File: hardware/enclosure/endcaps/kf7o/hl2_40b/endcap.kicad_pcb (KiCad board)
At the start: 2 copper layers, 106 x 40 mm, 14 parts, among them Q1 DTC144E, Q2 IRLML6402

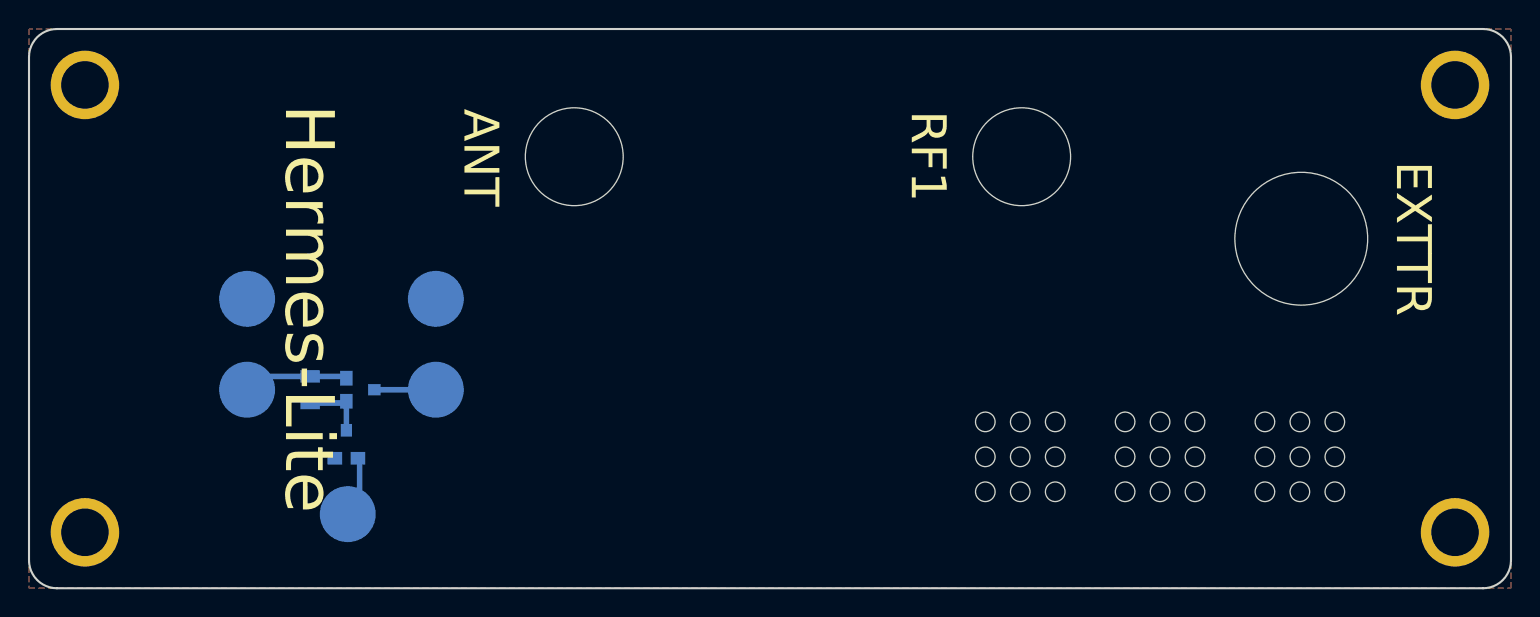
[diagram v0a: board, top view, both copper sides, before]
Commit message: Rev 2 of rear end plate
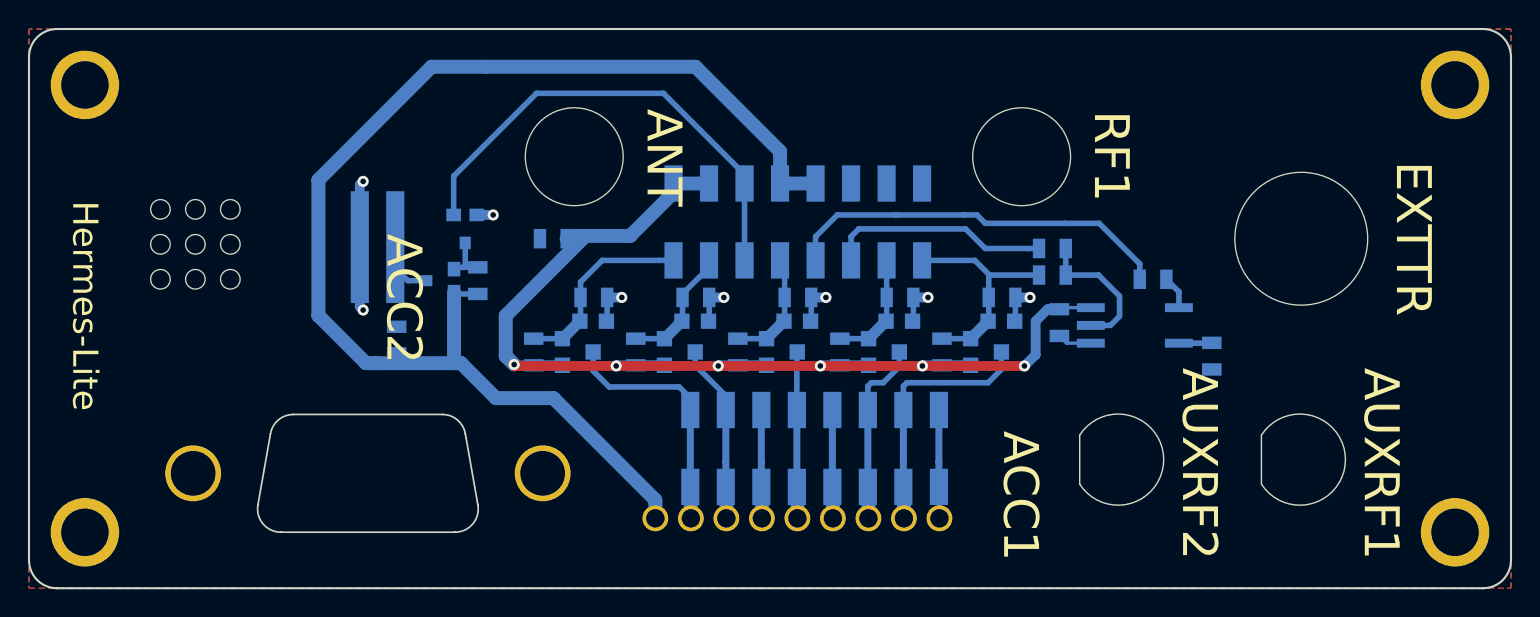
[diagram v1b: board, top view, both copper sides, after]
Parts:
- removed the REF** at (118.4, 83.1)
- removed TP1: Power, TestPoint:TestPoint_Pad_D4.0mm
- removed TP2: Fan Control, TestPoint:TestPoint_Pad_D4.0mm
- removed TP3, TP5: Ground, TestPoint:TestPoint_Pad_D4.0mm
- removed TP4: Fan Power, TestPoint:TestPoint_Pad_D4.0mm
- added ACC1: Terminal Block, endcaplib:terminal_block, B.Cu at (94.8, 85.0)
- added ACC2: DB9, endcaplib:DSUB-9_Cutout, B.Cu at (68.7, 83.2)
- added AUXRF1: SMA, endcaplib:sma_panel, B.Cu at (140.9, 80.8)
- added AUXRF2: SMA, endcaplib:sma_panel, B.Cu at (127.9, 80.8)
- added C1: 0.1uF, endcaplib:SMD-0805, B.Cu at (123.7, 71.0)
- added C2: 0.1uF, endcaplib:SMD-0805, B.Cu at (76.3, 72.2)
- added C3: 0.1uF, endcaplib:SMD-0805, B.Cu at (87.5, 65.0)
- added J2: Male Header, endcaplib:male_header, B.Cu at (96.1, 63.8)
- added J3: Male Header, endcaplib:male_header, B.Cu at (97.3, 80.0)
- added J4: Fan, endcaplib:male_header_2, B.Cu at (76.2, 65.6)
- added Q3: MULTIFET, endcaplib:3sot3_3, B.Cu at (91.3, 70.9)
- added Q4: MULTIFET, endcaplib:3sot3_3, B.Cu at (98.6, 70.9)
- added Q5: MULTIFET, endcaplib:3sot3_3, B.Cu at (105.9, 70.9)
- added Q6: MULTIFET, endcaplib:3sot3_3, B.Cu at (113.2, 70.9)
- added Q7: MULTIFET, endcaplib:3sot3_3, B.Cu at (120.5, 70.9)
- added R10: 10K, endcaplib:SMD-0805, B.Cu at (115.3, 73.1)
- added R11: 10K, endcaplib:SMD-0805, B.Cu at (119.6, 69.2)
- added R12: 1K, endcaplib:SMD-0805, B.Cu at (130.4, 67.9)
- added R13: 680, endcaplib:SMD-0805, B.Cu at (134.6, 73.4)
- added R14: 0, endcaplib:SMD-0805, B.Cu at (123.2, 65.7)
- added R15: 0, endcaplib:SMD-0805, B.Cu at (123.2, 67.6)
- added R2: 10K, endcaplib:SMD-0805, B.Cu at (86.1, 73.1)
- added R3: 10K, endcaplib:SMD-0805, B.Cu at (90.4, 69.2)
- added R4: 10K, endcaplib:SMD-0805, B.Cu at (93.4, 73.1)
- added R5: 10K, endcaplib:SMD-0805, B.Cu at (97.7, 69.2)
- added R6: 10K, endcaplib:SMD-0805, B.Cu at (100.7, 73.1)
- added R7: 10K, endcaplib:SMD-0805, B.Cu at (105.0, 69.2)
- added R8: 10K, endcaplib:SMD-0805, B.Cu at (108.0, 73.1)
- added R9: 10K, endcaplib:SMD-0805, B.Cu at (112.3, 69.2)
- added REF**: speakerventsmall, endcaplib:speakerventsmall, F.Cu at (59.4, 67.9)
- added U1: ACPL-M61M-500E, Package_SO:SO-5_4.4x3.6mm_P1.27mm, B.Cu at (129.1, 71.2)
- moved Q1 19.4 mm to (81.2, 63.3), turned to 0 degrees
- moved R1 14.3 mm to (82.1, 68.0), turned to 90 degrees
- moved Q2 11.0 mm to (80.4, 68.0), turned to 270 degrees
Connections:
- net Earth renamed GNDS
- net Net-(Q2-Pad2) renamed VSUP
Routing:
- net Vlvds: track 0.00 -> 85.9 mm, vias 0 -> 6
- net VSUP: track 7.50 -> 91.7 mm
- net GNDS: track 0.00 -> 34.7 mm, vias 0 -> 8
- net Net-(J2-Pad5): track 4.35 -> 34.6 mm
- net ISOIN: track 0.00 -> 28.1 mm
- net Net-(ACC1-Pad8): track 0.00 -> 18.2 mm
- net Net-(J2-Pad16): track 0.00 -> 18.1 mm
- net Net-(ACC1-Pad2): track 0.00 -> 17.7 mm
- net Net-(J2-Pad12): track 0.00 -> 16.0 mm
- net Net-(J2-Pad2): track 0.00 -> 15.1 mm
- net Net-(ACC1-Pad7): track 0.00 -> 13.3 mm
- net Net-(ACC1-Pad3): track 0.00 -> 12.8 mm
- net Net-(ACC1-Pad5): track 0.00 -> 11.9 mm
- net Net-(R14-Pad2): track 0.00 -> 10.1 mm
- net Net-(J2-Pad8): track 0.00 -> 9.52 mm
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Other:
- board text added: "ACC1"
- board text added: "ACC2"
- board text added: "AUXRF1"
- board text added: "AUXRF2"
